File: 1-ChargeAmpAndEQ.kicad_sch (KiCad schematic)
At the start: 56 parts, among them J101 6.3mm stereo, J102 6.3mm stereo, U101 OPA145, U102 OPA145

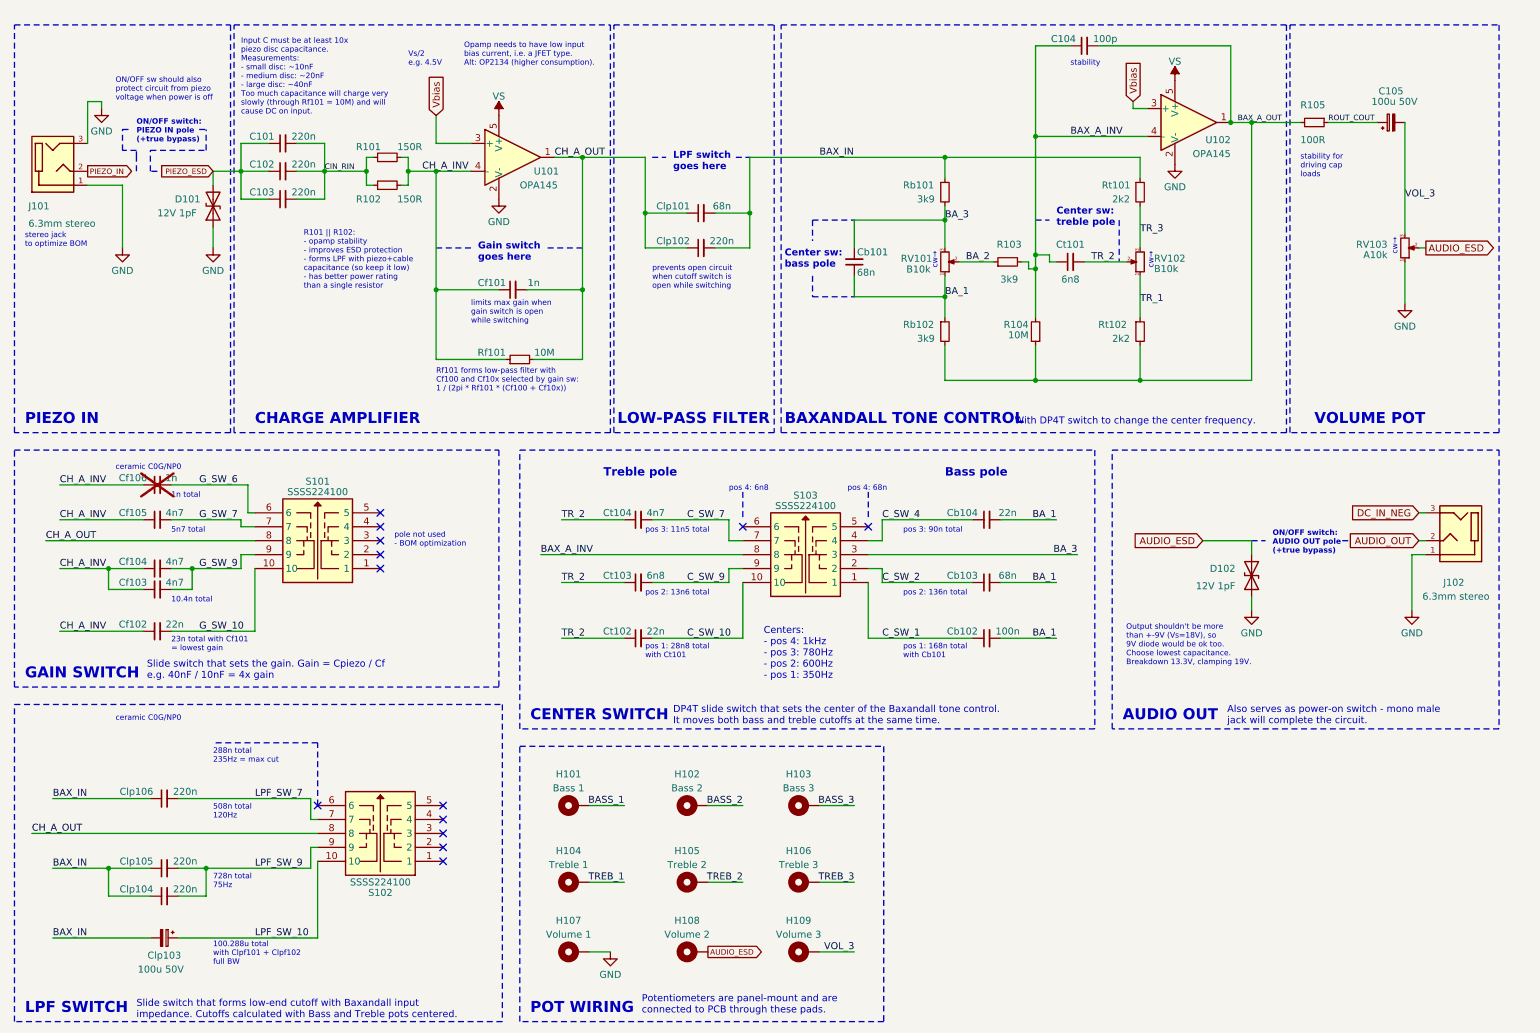
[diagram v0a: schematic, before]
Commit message: schematics: replacing the switches, rewiring, improving center switch positions, removing 6n8 cap
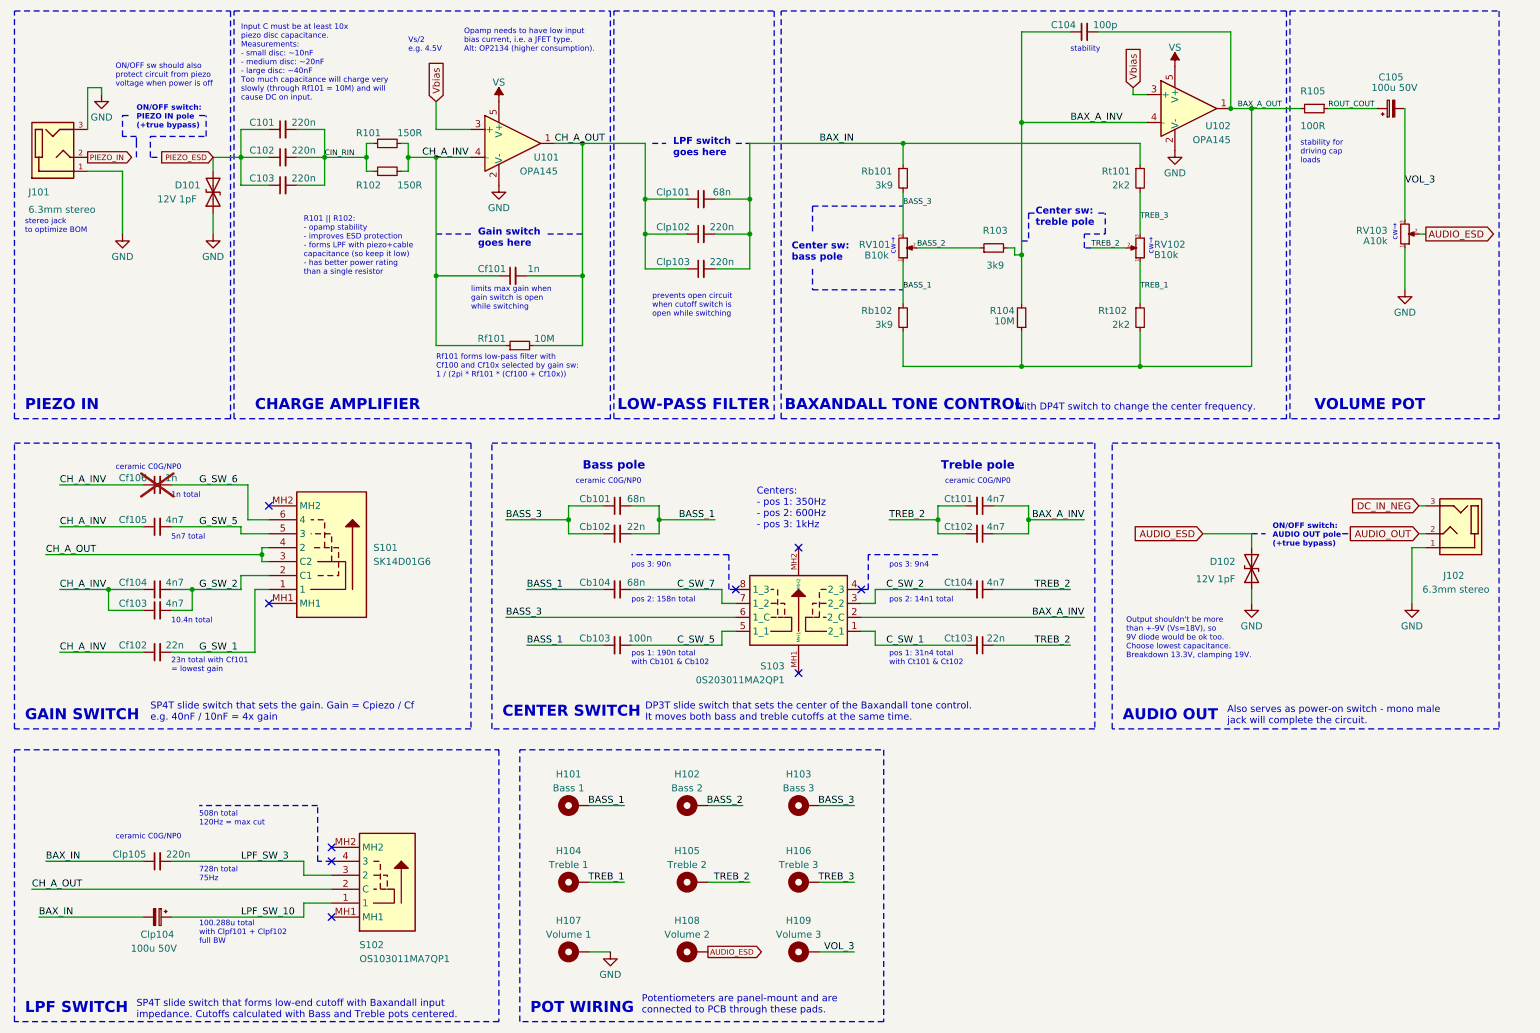
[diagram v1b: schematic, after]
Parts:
- removed Cb104: 22n, library:GRM21B5C1H223JA01L, symbol Device:C_Small
- removed Clp104: 220n, library:GRM31C5C1H224JE02L, symbol Device:C_Small
- removed Ct103: 6n8, library:GRM1885C1H682JA01D, symbol Device:C_Small
- removed S101, S102, S103: SSSS224100, library:SSSS224100, symbol SSSS224100:SSSS224100
- added Cb102: 22n, library:GRM21B5C1H223JA01L, symbol Device:C_Small
- added Ct102: 4n7, library:GRM1885C1H472JA01D, symbol Device:C_Small
- added S101: SK14D01G6, library:sw_SK14D01G6, symbol sw_SK14D01G6:SK14D01G6
- added S102: OS103011MA7QP1, library:sw_OS103011MA7QP1, symbol sw_OS103011MA7QP1:OS103011MA7QP1
- added S103: 0S203011MA2QP1, library:sw_0S203011MA2QP1, symbol sw_0S203011MA2QP1:0S203011MA2QP1
- Ct101: value 6n8 -> 4n7; footprint library:GRM1885C1H682JA01D -> library:GRM1885C1H472JA01D; LCSC Part # C162241 -> C85980; Mfr Part # GRM1885C1H682JA01D -> GRM1885C1H472JA01D; Mouser Part # 81-GRM1885C1H682JA1D -> 81-GRM1885C1H472JA1D
- renumbered Cb102 to Cb103, Cb103 to Cb104, Clp106 to Clp103, Clp103 to Clp104, Ct102 to Ct103
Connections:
- net BA_2 is gone; now on net BASS_2: R103.1, RV101.2
- net C_SW_10 is gone; now on net C_SW_1: Ct103.2
- net LPF_SW_7 is gone; now on net BAX_IN: Clp103.2
- net TR_1 is gone; now on net TREB_1: RV102.1, Rt102.1
- net TR_2 is gone; now on net TREB_2: Ct101.2, Ct103.1, Ct104.1, RV102.2
- net TR_3 is gone; now on net TREB_3: RV102.3, Rt101.2
- net BASS_1: now also Cb101.2, Cb103.2, Cb104.2, RV101.1, Rb102.1, Cb102.1
- net BASS_3: now also Cb101.1, RV101.3, Rb101.2, Cb102.2, S103.6 (1_C)
- net BAX_A_INV: now also Ct102.1, S103.2 (2_C)
- net BAX_IN: no longer Clp103.1
- net CH_A_OUT: now also Clp103.1, S101.3 (C2), S101.4 (2), S102.2 (C)
- net C_SW_1: now also S103.1 (2_1); no longer Cb103.1
- net C_SW_2: now also Ct104.2, S103.3 (2_2); no longer Cb104.1
- net C_SW_7: now also Cb104.1, S103.7 (1_2); no longer Ct104.2
- net G_SW_6: now also S101.6 (4)
- net LPF_SW_10: now also S102.1
- net TREB_2: now also Ct102.2
- removed net BA_1: Cb101.1, Cb103.2, Cb104.2, RV101.1, Rb102.1
- removed net BA_3: Cb101.2, RV101.3, Rb101.2
- net G_SW_10 renamed G_SW_1
- net G_SW_1: now also S101.1
- net G_SW_7 renamed G_SW_5
- net G_SW_5: now also S101.5 (3)
- net G_SW_9 renamed G_SW_2
- net G_SW_2: now also S101.2 (C1)
- net LPF_SW_9 renamed LPF_SW_3
- net LPF_SW_3: now also S102.3 (2)
- new net C_SW_5: Cb103.1, S103.5 (1_1)
- no-connect marks 13 -> 9
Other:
- note added: "508n total 120Hz = max cut"
- note added: "Centers: - pos 1: 350Hz - pos 2: 600Hz - pos 3: 1kHz"
- note added: "DP3T slide switch that sets the center of the Baxandall tone control. It moves both bass and treble cutoffs at the same time."
- note added: "SP4T slide switch that forms low-end cutoff with Baxandall input impedance. Cutoffs calculated with Bass and Treble pots centered."
- note added: "SP4T slide switch that sets the gain. Gain = Cpiezo / Cf e.g. 40nF / 10nF = 4x gain"
- note added: "pos 1: 190n total with Cb101 & Cb102"
- note added: "pos 1: 31n4 total with Ct101 & Ct102"
- note added: "pos 2: 14n1 total"
- note added: "pos 2: 158n total"
- note added: "pos 3: 90n"
- note added: "pos 3: 9n4"
- note removed: "288n total 235Hz = max cut"
- note removed: "508n total 120Hz"
- note removed: "Centers: - pos 4: 1kHz - pos 3: 780Hz - pos 2: 600Hz - pos 1: 350Hz"
- note removed: "DP4T slide switch that sets the center of the Baxandall tone control. It moves both bass and treble cutoffs at the same time."
- note removed: "Slide switch that forms low-end cutoff with Baxandall input impedance. Cutoffs calculated with Bass and Treble pots centered."
- note removed: "Slide switch that sets the gain. Gain = Cpiezo / Cf e.g. 40nF / 10nF = 4x gain"
- note removed: "pole not used - BOM optimization"
- note removed: "pos 1: 168n total with Cb101"
- note removed: "pos 1: 28n8 total with Ct101"
- note removed: "pos 2: 136n total"
- note removed: "pos 2: 13n6 total"
- note removed: "pos 3: 11n5 total"
- note removed: "pos 3: 90n total"
- note removed: "pos 4: 68n"
- note removed: "pos 4: 6n8"
- moved on the sheet: C101, C102, C103, C104, C105, Cb101, Cb103, Cb104, Cf101, Cf102, Cf103, Cf104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

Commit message: schematic: renaming low-pass filter to high-pass filter as it was named incorrectly lol
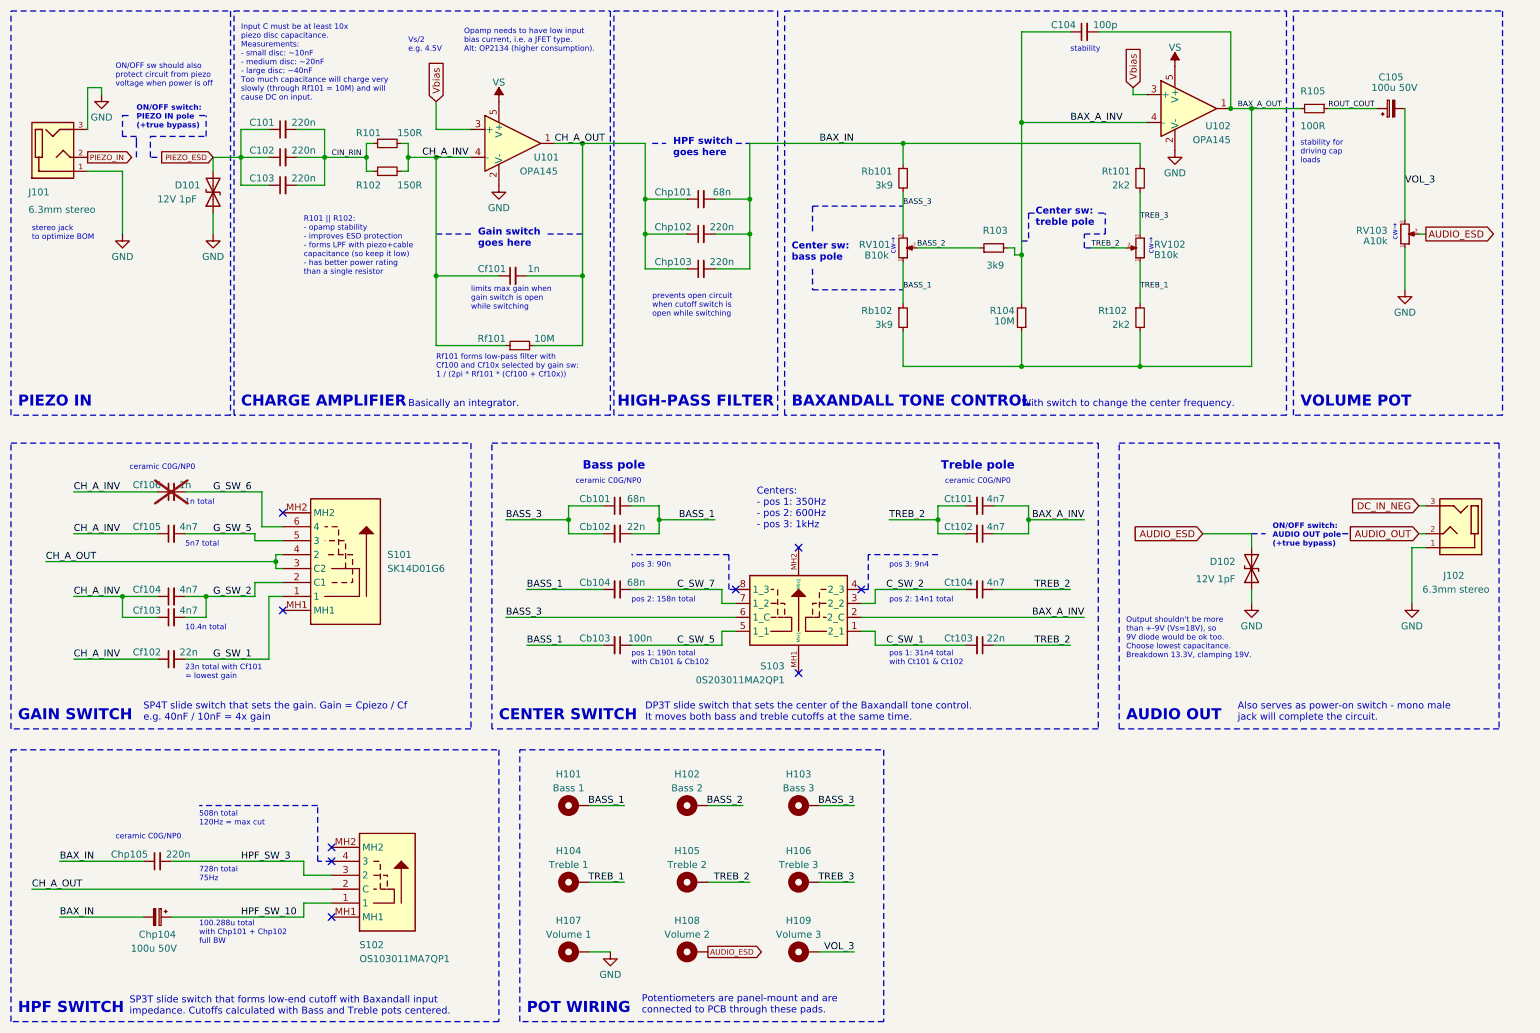
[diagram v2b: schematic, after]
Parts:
- Chp101: renamed from Clp101; Purpose LPF - sets low-pass cutoff frequency -> HPF - sets high-pass cutoff frequency
- Chp102: renamed from Clp102; Purpose LPF - sets low-pass cutoff frequency -> HPF - sets high-pass cutoff frequency
- Chp103: renamed from Clp103; Purpose LPF - sets low-pass cutoff frequency -> HPF - sets high-pass cutoff frequency
- Chp104: renamed from Clp104; Purpose AC coupling / DC blocking -> HPF - sets high-pass cutoff frequency
- Chp105: renamed from Clp105; Purpose LPF - sets low-pass cutoff frequency -> HPF - sets high-pass cutoff frequency
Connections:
- net LPF_SW_10 renamed HPF_SW_10
- net LPF_SW_3 renamed HPF_SW_3
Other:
- note added: "100.288u total with Chp101 + Chp102 full BW"
- note added: "Basically an integrator."
- note added: "HIGH-PASS FILTER"
- note added: "HPF SWITCH"
- note added: "HPF switch goes here"
- note added: "SP3T slide switch that forms low-end cutoff with Baxandall input impedance. Cutoffs calculated with Bass and Treble pots centered."
- note added: "With switch to change the center frequency."
- note removed: "100.288u total with Clpf101 + Clpf102 full BW"
- note removed: "LOW-PASS FILTER"
- note removed: "LPF SWITCH"
- note removed: "LPF switch goes here"
- note removed: "SP4T slide switch that forms low-end cutoff with Baxandall input impedance. Cutoffs calculated with Bass and Treble pots centered."
- note removed: "With DP4T switch to change the center frequency."
- moved on the sheet: Cf102, Cf103, Cf104, Cf105, Cf106, S101

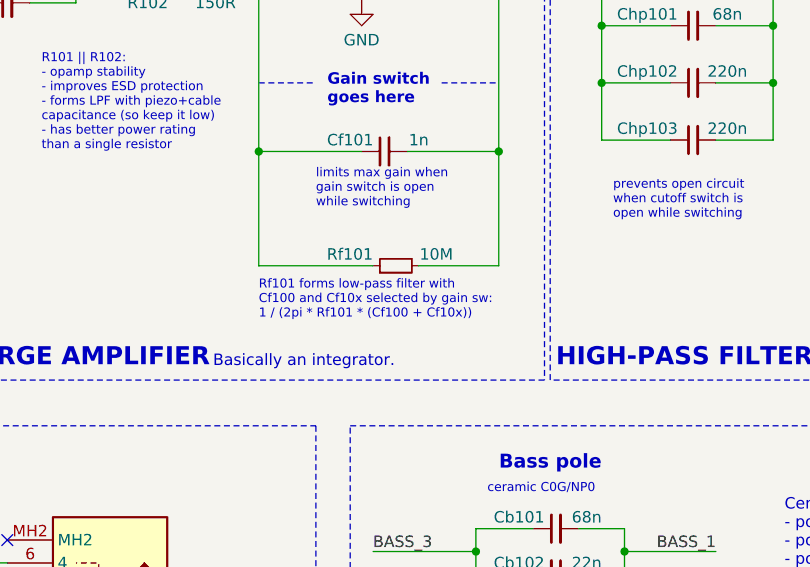
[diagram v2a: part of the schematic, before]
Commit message: updating the board and remaining low-pass references in schematic
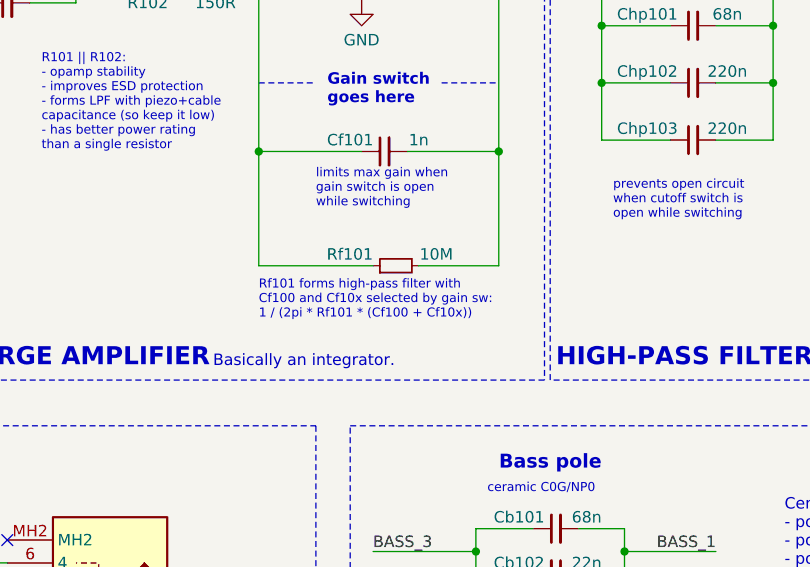
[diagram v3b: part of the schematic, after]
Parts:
- Rf101: Purpose charge amp feedback resistor - sets LP cutoff with feedback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 -> charge amp feedback resistor - sets high-pass cutoff with f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
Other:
- note added: "Rf101 forms high-pass filter with Cf100 and Cf10x selected by gain sw: 1 / (2pi * Rf101 * (Cf100 + Cf10x))"
- note removed: "Rf101 forms low-pass filter with Cf100 and Cf10x selected by gain sw: 1 / (2pi * Rf101 * (Cf100 + Cf10x))"
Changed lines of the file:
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@@
 		)
 	)
-	(text "Rf101 forms low-pass filter with\nCf100 and Cf10x selected by gain sw:\n1 / (2pi * Rf101 * (Cf100 + Cf10x))\n\n"
+	(text "Rf101 forms high-pass filter with\nCf100 and Cf10x selected by gain sw:\n1 / (2pi * Rf101 * (Cf100 + Cf10x))\n\n"
 		(exclude_from_sim no)
 		(at 90.17 81.28 0)
@@
 			)
 		)
-		(property "Purpose" "charge amp feedback resistor - sets LP cutoff with feedback capacitance"
+		(property "Purpose" "charge amp feedback resistor - sets high-pass cutoff with feedback capacitance"
 			(at 105.41 73.66 0)
 			(effects
